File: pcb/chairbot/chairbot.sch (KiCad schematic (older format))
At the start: 18 parts, among them J1 Conn_01x02, J2 Conn_01x05, U1 ESP32mini, U2 74HCT08, U3 74HCT244, U4 buck-converter, U5 nRF24L01+, U8 AMS1117-3.3, U9 PCA9515

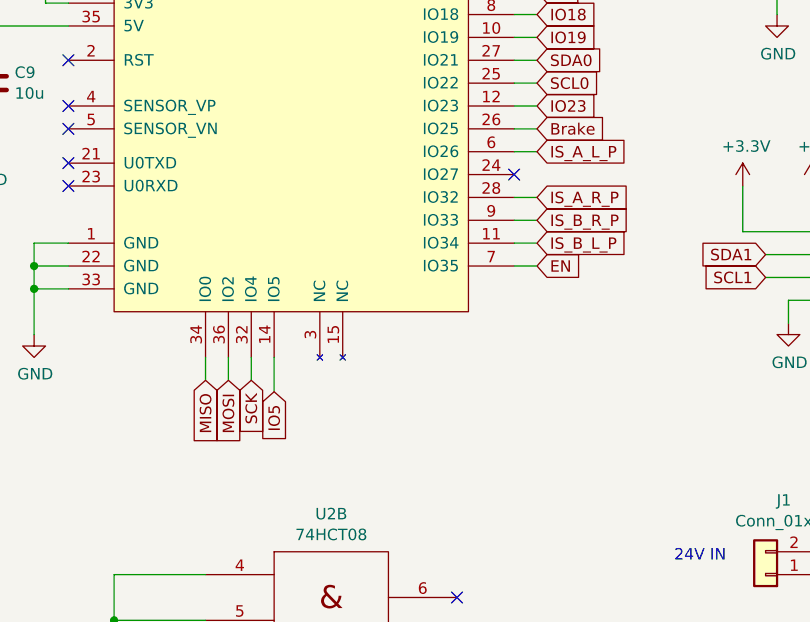
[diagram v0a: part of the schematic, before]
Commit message: Move MISO from IO0 to IO27.
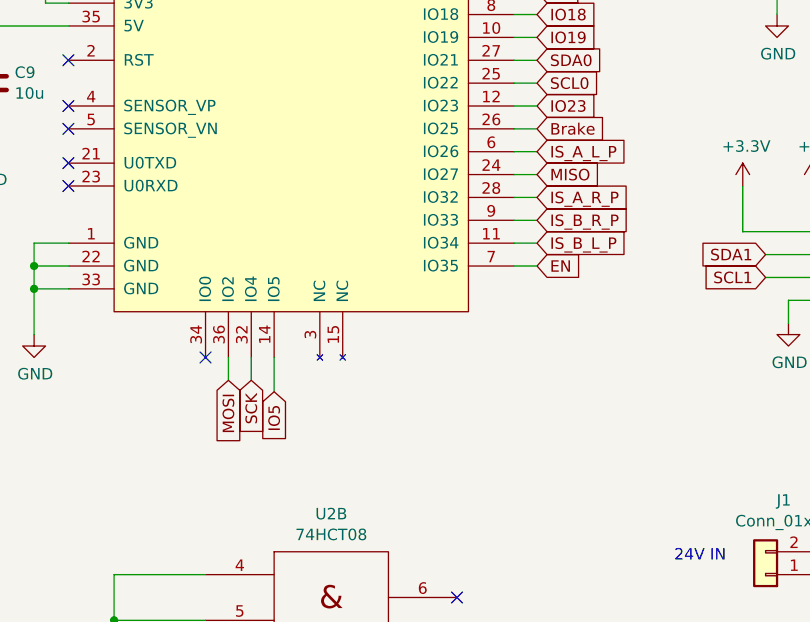
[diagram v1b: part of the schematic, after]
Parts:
- D1: footprint Diode_SMD:D_SMC -> Diode_SMD:D_SMB
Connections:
- net MISO: now also U1.24 (IO27); no longer U1.34 (IO0)
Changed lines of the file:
@@
 F 0 "D1" V 6004 5529 50  0000 L CNN
 F 1 "SS34" V 6095 5529 50  0000 L CNN
-F 2 "Diode_SMD:D_SMC" H 6050 5450 50  0001 C CNN
+F 2 "Diode_SMD:D_SMB" H 6050 5450 50  0001 C CNN
 F 3 "~" H 6050 5450 50  0001 C CNN
 	1    6050 5450
@@
 Text GLabel 2900 4500 3    50   Input ~ 0
 MOSI
-Text GLabel 2800 4500 3    50   Input ~ 0
+Text GLabel 4250 3600 2    50   Input ~ 0
 MISO
 Text GLabel 3000 4500 3    50   Input ~ 0
@@
 	4150 2700 4250 2700
 Wire Wire Line
-	2800 4400 2800 4500
-Wire Wire Line
 	2900 4400 2900 4500
 Wire Wire Line
@@
 NoConn ~ 2200 3550
 NoConn ~ 2200 3650
-NoConn ~ 4150 3600
 $Comp
 L power:+5V #PWR0125
@@
 Wire Wire Line
 	4250 3700 4150 3700
+Wire Wire Line
+	4250 3600 4150 3600
+NoConn ~ 2800 4400
 $EndSCHEMATC

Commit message: Fix various issues.
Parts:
- removed F1: Fuse, Resistor_THT:R_Axial_DIN0309_L9.0mm_D3.2mm_P2.54mm_Vertical, symbol Device:Fuse
- added C11: 100n, Capacitor_SMD:C_0603_1608Metric, symbol Device:C
- added R3: 10K, Resistor_SMD:R_0603_1608Metric, symbol Device:R
- added R4: 1K, Resistor_SMD:R_0603_1608Metric, symbol Device:R
- added R5: 2K2, Resistor_SMD:R_0603_1608Metric, symbol Device:R
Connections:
- net +24V: now also R3.1
- net Brake: now also U1.21 (U0TXD); no longer U1.26 (IO25)
- net EN: now also R5.1
- net GND: now also C11.2, R4.2, R5.2; no longer D1.2 (A)
- net at J1.2 (Pin_2): now also D1.2 (A)
- new net Vbat: C11.1, R3.2, R4.1, U1.26 (IO25)
- no-connect marks 24 -> 23
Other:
- moved on the sheet: C9, D1
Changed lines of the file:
@@
 	5450 5350 5550 5350
 $Comp
-L Device:Fuse F1
-U 1 1 5BD26A01
+L Device:D_Schottky D1
+U 1 1 5BD26B72
 P 5750 5250
-F 0 "F1" V 5553 5250 50  0000 C CNN
-F 1 "Fuse" V 5644 5250 50  0000 C CNN
-F 2 "Resistor_THT:R_Axial_DIN0309_L9.0mm_D3.2mm_P2.54mm_Vertical" V 5680 5250 50  0001 C CNN
+F 0 "D1" V 5704 5329 50  0000 L CNN
+F 1 "SS34" V 5795 5329 50  0000 L CNN
+F 2 "Diode_SMD:D_SMB" H 5750 5250 50  0001 C CNN
 F 3 "~" H 5750 5250 50  0001 C CNN
 	1    5750 5250
-	0    1    1    0
-$EndComp
-$Comp
-L Device:D_Schottky D1
-U 1 1 5BD26B72
-P 6050 5450
-F 0 "D1" V 6004 5529 50  0000 L CNN
-F 1 "SS34" V 6095 5529 50  0000 L CNN
-F 2 "Diode_SMD:D_SMB" H 6050 5450 50  0001 C CNN
-F 3 "~" H 6050 5450 50  0001 C CNN
-	1    6050 5450
-	0    1    1    0
+	-1   0    0    1
 $EndComp
 Wire Wire Line
 	5550 5350 5550 5650
-Wire Wire Line
-	6050 5600 6050 5650
-Wire Wire Line
-	6050 5650 5550 5650
 Connection ~ 5550 5650
 Wire Wire Line
@@
 Wire Wire Line
 	5450 5250 5600 5250
-Wire Wire Line
-	5900 5250 6050 5250
-Wire Wire Line
-	6050 5250 6050 5300
 $Comp
 L power:+24V #PWR03
@@
 	1    0    0    -1
 $EndComp
-Connection ~ 6050 5250
 $Comp
 L buckconverter:buck-converter U4
@@
 	6550 5500 6850 5500
 Wire Wire Line
-	6050 5250 6550 5250
-Wire Wire Line
 	6550 5050 6550 5250
 Connection ~ 6550 5250
-Wire Wire Line
-	6050 5650 6850 5650
-Connection ~ 6050 5650
 $Comp
 L power:+5V #PWR06
@@
 Text GLabel 4250 4000 2    50   Input ~ 0
 EN
-Text GLabel 4250 3400 2    50   Input ~ 0
+Text GLabel 2050 3550 0    50   Input ~ 0
 Brake
 $Comp
@@
 L Device:C C9
 U 1 1 5BD55B4E
-P 1850 3200
-F 0 "C9" H 1965 3246 50  0000 L CNN
-F 1 "10u" H 1965 3155 50  0000 L CNN
-F 2 "Capacitor_SMD:C_0805_2012Metric" H 1888 3050 50  0001 C CNN
-F 3 "~" H 1850 3200 50  0001 C CNN
-	1    1850 3200
+P 1500 3200
+F 0 "C9" H 1615 3246 50  0000 L CNN
+F 1 "10u" H 1615 3155 50  0000 L CNN
+F 2 "Capacitor_SMD:C_0805_2012Metric" H 1538 3050 50  0001 C CNN
+F 3 "~" H 1500 3200 50  0001 C CNN
+	1    1500 3200
 	1    0    0    -1
 $EndComp
@@
 L power:+5V #PWR0122
 U 1 1 5BD55BFD
-P 1850 2850
-F 0 "#PWR0122" H 1850 2700 50  0001 C CNN
-F 1 "+5V" H 1865 3023 50  0000 C CNN
-F 2 "" H 1850 2850 50  0001 C CNN
-F 3 "" H 1850 2850 50  0001 C CNN
-	1    1850 2850
-	1    0    0    -1
-$EndComp
-Wire Wire Line
-	1850 2850 1850 2950
-Wire Wire Line
-	2200 2950 1850 2950
-Connection ~ 1850 2950
-Wire Wire Line
-	1850 2950 1850 3050
+P 1500 2850
+F 0 "#PWR0122" H 1500 2700 50  0001 C CNN
+F 1 "+5V" H 1515 3023 50  0000 C CNN
+F 2 "" H 1500 2850 50  0001 C CNN
+F 3 "" H 1500 2850 50  0001 C CNN
+	1    1500 2850
+	1    0    0    -1
+$EndComp
+Wire Wire Line
+	1500 2850 1500 2950
+Connection ~ 1500 2950
+Wire Wire Line
+	1500 2950 1500 3050
 $Comp
 L power:GND #PWR0123
 U 1 1 5BD59785
-P 1850 3450
-F 0 "#PWR0123" H 1850 3200 50  0001 C CNN
-F 1 "GND" H 1855 3277 50  0000 C CNN
-F 2 "" H 1850 3450 50  0001 C CNN
-F 3 "" H 1850 3450 50  0001 C CNN
-	1    1850 3450
-	1    0    0    -1
-$EndComp
-Wire Wire Line
-	1850 3450 1850 3350
+P 1500 3450
+F 0 "#PWR0123" H 1500 3200 50  0001 C CNN
+F 1 "GND" H 1505 3277 50  0000 C CNN
+F 2 "" H 1500 3450 50  0001 C CNN
+F 3 "" H 1500 3450 50  0001 C CNN
+	1    1500 3450
+	1    0    0    -1
+$EndComp
+Wire Wire Line
+	1500 3450 1500 3350
 $Comp
 L power:+3.3V #PWR0124
@@
 Wire Wire Line
 	4150 3400 4250 3400
-NoConn ~ 2200 3550
 NoConn ~ 2200 3650
 $Comp
@@
 	4250 3600 4150 3600
 NoConn ~ 2800 4400
+Wire Wire Line
+	1500 2950 2200 2950
+Wire Wire Line
+	2050 3550 2200 3550
+Text GLabel 4250 3400 2    50   Input ~ 0
+Vbat
+$Comp
+L Device:R R3
+U 1 1 5CB47065
+P 1250 5900
+F 0 "R3" H 1320 5946 50  0000 L CNN
+F 1 "10K" H 1320 5855 50  0000 L CNN
+F 2 "Resistor_SMD:R_0603_1608Metric" V 1180 5900 50  0001 C CNN
+F 3 "~" H 1250 5900 50  0001 C CNN
+	1    1250 5900
+	1    0    0    -1
+$EndComp
+$Comp
+L Device:R R4
+U 1 1 5CB470D2
+P 1250 6500
+F 0 "R4" H 1320 6546 50  0000 L CNN
+F 1 "1K" H 1320 6455 50  0000 L CNN
+F 2 "Resistor_SMD:R_0603_1608Metric" V 1180 6500 50  0001 C CNN
+F 3 "~" H 1250 6500 50  0001 C CNN
+	1    1250 6500
+	1    0    0    -1
+$EndComp
+$Comp
+L power:+24V #PWR011
+U 1 1 5CB4717B
+P 1250 5550
+F 0 "#PWR011" H 1250 5400 50  0001 C CNN
+F 1 "+24V" H 1265 5723 50  0000 C CNN
+F 2 "" H 1250 5550 50  0001 C CNN
+F 3 "" H 1250 5550 50  0001 C CNN
+	1    1250 5550
+	1    0    0    -1
+$EndComp
+$Comp
+L power:GND #PWR012
+U 1 1 5CB47209
+P 1250 6950
+F 0 "#PWR012" H 1250 6700 50  0001 C CNN
+F 1 "GND" H 1255 6777 50  0000 C CNN
+F 2 "" H 1250 6950 50  0001 C CNN
+F 3 "" H 1250 6950 50  0001 C CNN
+	1    1250 6950
+	1    0    0    -1
+$EndComp
+$Comp
+L Device:C C11
+U 1 1 5CB47282
+P 850 6500
+F 0 "C11" H 965 6546 50  0000 L CNN
+F 1 "100n" H 965 6455 50  0000 L CNN
+F 2 "Capacitor_SMD:C_0603_1608Metric" H 888 6350 50  0001 C CNN
+F 3 "~" H 850 6500 50  0001 C CNN
+	1    850  6500
+	1    0    0    -1
+$EndComp
+Wire Wire Line
+	1250 6050 1250 6200
+Wire Wire Line
+	850  6350 850  6200
+Wire Wire Line
+	850  6200 1250 6200
+Connection ~ 1250 6200
+Wire Wire Line
+	1250 6200 1250 6350
+Wire Wire Line
+	1250 5550 1250 5750
+Wire Wire Line
+	1250 6650 1250 6800
+Wire Wire Line
+	850  6650 850  6800
+Wire Wire Line
+	850  6800 1250 6800
+Connection ~ 1250 6800
+Wire Wire Line
+	1250 6800 1250 6950
+Text GLabel 1500 6200 2    50   Input ~ 0
+Vbat
+Wire Wire Line
+	1500 6200 1250 6200
+$Comp
+L Device:R R5
+U 1 1 5CB60365
+P 4150 4400
+F 0 "R5" H 4220 4446 50  0000 L CNN
+F 1 "2K2" H 4220 4355 50  0000 L CNN
+F 2 "Resistor_SMD:R_0603_1608Metric" V 4080 4400 50  0001 C CNN
+F 3 "~" H 4150 4400 50  0001 C CNN
+	1    4150 4400
+	1    0    0    -1
+$EndComp
+$Comp
+L power:GND #PWR013
+U 1 1 5CB60409
+P 4150 4700
+F 0 "#PWR013" H 4150 4450 50  0001 C CNN
+F 1 "GND" H 4155 4527 50  0000 C CNN
+F 2 "" H 4150 4700 50  0001 C CNN
+F 3 "" H 4150 4700 50  0001 C CNN
+	1    4150 4700
+	1    0    0    -1
+$EndComp
+Wire Wire Line
+	4150 4700 4150 4550
+Wire Wire Line
+	4150 4000 4150 4250
+Connection ~ 4150 4000
+Wire Wire Line
+	5900 5250 6550 5250
+Wire Wire Line
+	5550 5650 6850 5650
 $EndSCHEMATC

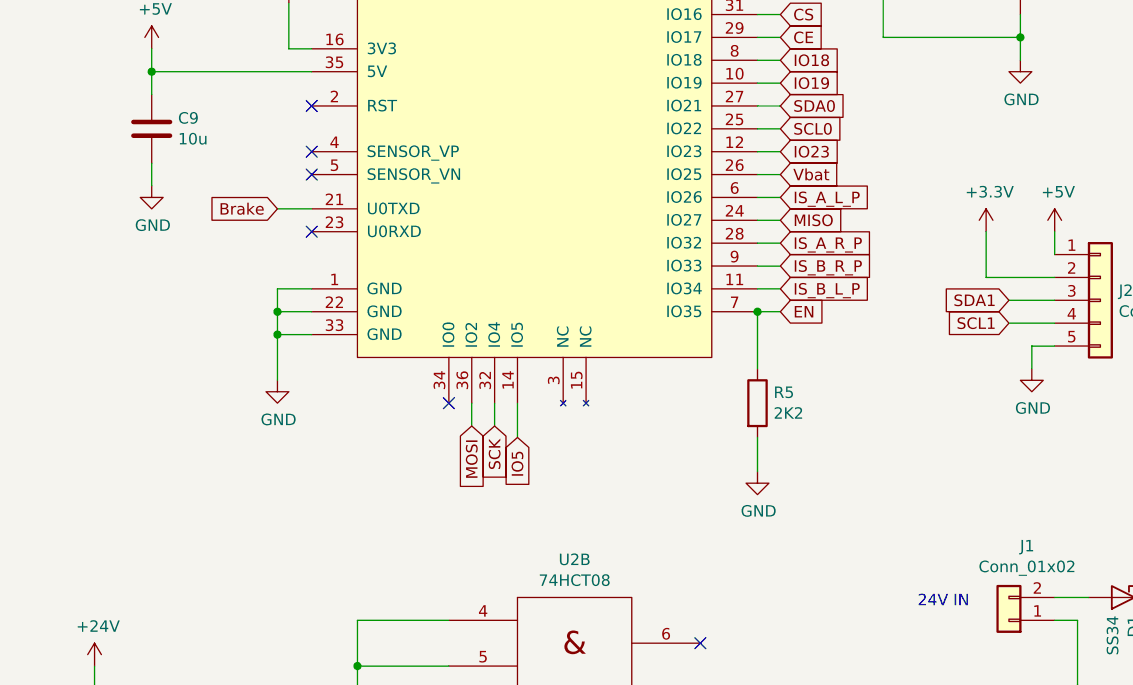
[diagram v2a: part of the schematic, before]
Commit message: Tweak pin numbers.
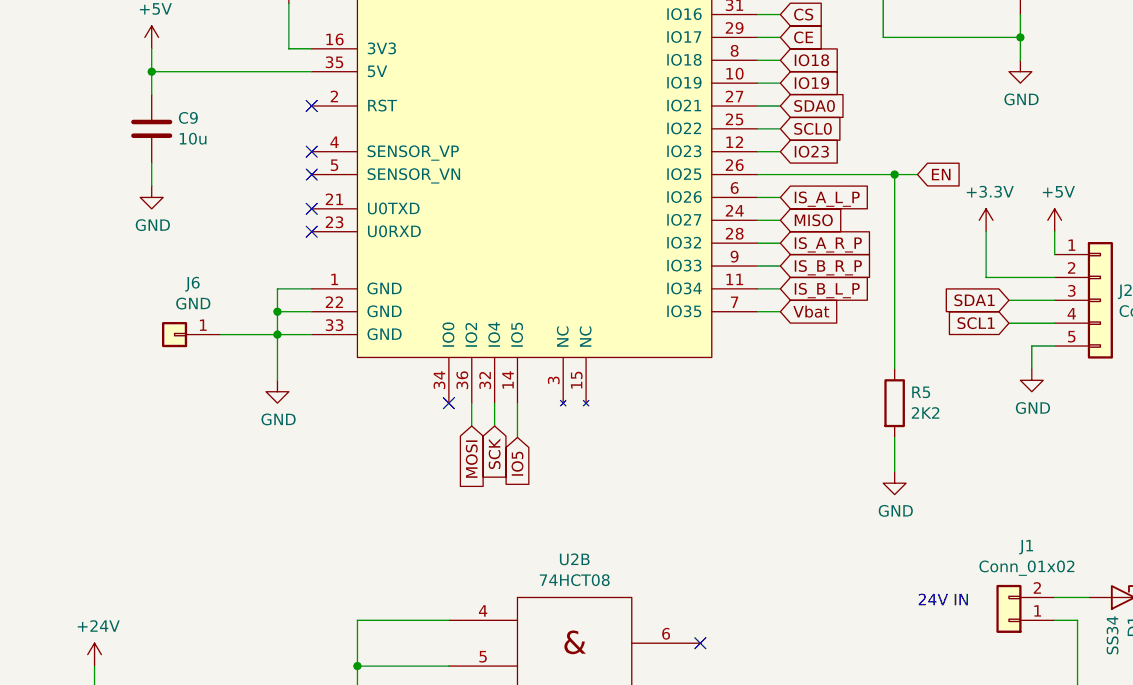
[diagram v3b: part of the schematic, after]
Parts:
- added J6: GND, Connector_Pin:Pin_D1.3mm_L11.0mm, symbol Connector_Generic:Conn_01x01
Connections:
- net EN: now also U1.26 (IO25); no longer U1.7 (IO35)
- net GND: now also J6.1 (Pin_1)
- net Vbat: now also U1.7 (IO35); no longer U1.26 (IO25)
- net Brake: no longer names the net of U1.21 (U0TXD)
- no-connect marks 23 -> 24
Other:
- moved on the sheet: R5
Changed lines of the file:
@@
 EESchema Schematic File Version 4
 LIBS:chairbot-cache
-EELAYER 26 0
+EELAYER 29 0
 EELAYER END
 $Descr A4 11693 8268
@@
 Text GLabel 4250 2800 2    50   Input ~ 0
 CE
-Text GLabel 4250 4000 2    50   Input ~ 0
+Text GLabel 4850 3400 2    50   Input ~ 0
 EN
-Text GLabel 2050 3550 0    50   Input ~ 0
-Brake
 $Comp
 L Regulator_Linear:AMS1117-3.3 U8
@@
 Wire Wire Line
 	4250 4000 4150 4000
-Wire Wire Line
-	4150 3400 4250 3400
 NoConn ~ 2200 3650
 $Comp
@@
 Wire Wire Line
 	1500 2950 2200 2950
-Wire Wire Line
-	2050 3550 2200 3550
-Text GLabel 4250 3400 2    50   Input ~ 0
+Text GLabel 4250 4000 2    50   Input ~ 0
 Vbat
 $Comp
@@
 L Device:R R5
 U 1 1 5CB60365
-P 4150 4400
-F 0 "R5" H 4220 4446 50  0000 L CNN
-F 1 "2K2" H 4220 4355 50  0000 L CNN
-F 2 "Resistor_SMD:R_0603_1608Metric" V 4080 4400 50  0001 C CNN
-F 3 "~" H 4150 4400 50  0001 C CNN
-	1    4150 4400
+P 4750 4400
+F 0 "R5" H 4820 4446 50  0000 L CNN
+F 1 "2K2" H 4820 4355 50  0000 L CNN
+F 2 "Resistor_SMD:R_0603_1608Metric" V 4680 4400 50  0001 C CNN
+F 3 "~" H 4750 4400 50  0001 C CNN
+	1    4750 4400
 	1    0    0    -1
 $EndComp
@@
 L power:GND #PWR013
 U 1 1 5CB60409
-P 4150 4700
-F 0 "#PWR013" H 4150 4450 50  0001 C CNN
-F 1 "GND" H 4155 4527 50  0000 C CNN
-F 2 "" H 4150 4700 50  0001 C CNN
-F 3 "" H 4150 4700 50  0001 C CNN
-	1    4150 4700
-	1    0    0    -1
-$EndComp
-Wire Wire Line
-	4150 4700 4150 4550
-Wire Wire Line
-	4150 4000 4150 4250
-Connection ~ 4150 4000
+P 4750 4700
+F 0 "#PWR013" H 4750 4450 50  0001 C CNN
+F 1 "GND" H 4755 4527 50  0000 C CNN
+F 2 "" H 4750 4700 50  0001 C CNN
+F 3 "" H 4750 4700 50  0001 C CNN
+	1    4750 4700
+	1    0    0    -1
+$EndComp
+Wire Wire Line
+	4750 4700 4750 4550
 Wire Wire Line
 	5900 5250 6550 5250
 Wire Wire Line
 	5550 5650 6850 5650
+Wire Wire Line
+	4150 3400 4750 3400
+Wire Wire Line
+	4750 4250 4750 3400
+Connection ~ 4750 3400
+Wire Wire Line
+	4750 3400 4850 3400
+NoConn ~ 2200 3550
+$Comp
+L Connector_Generic:Conn_01x01 J6
+U 1 1 5CCFD0F5
+P 1600 4100
+F 0 "J6" H 1518 3875 50  0000 C CNN
+F 1 "GND" H 1518 3966 50  0000 C CNN
+F 2 "Connector_Pin:Pin_D1.3mm_L11.0mm" H 1600 4100 50  0001 C CNN
+F 3 "~" H 1600 4100 50  0001 C CNN
+	1    1600 4100
+	-1   0    0    1
+$EndComp
+Wire Wire Line
+	1800 4100 2050 4100
 $EndSCHEMATC

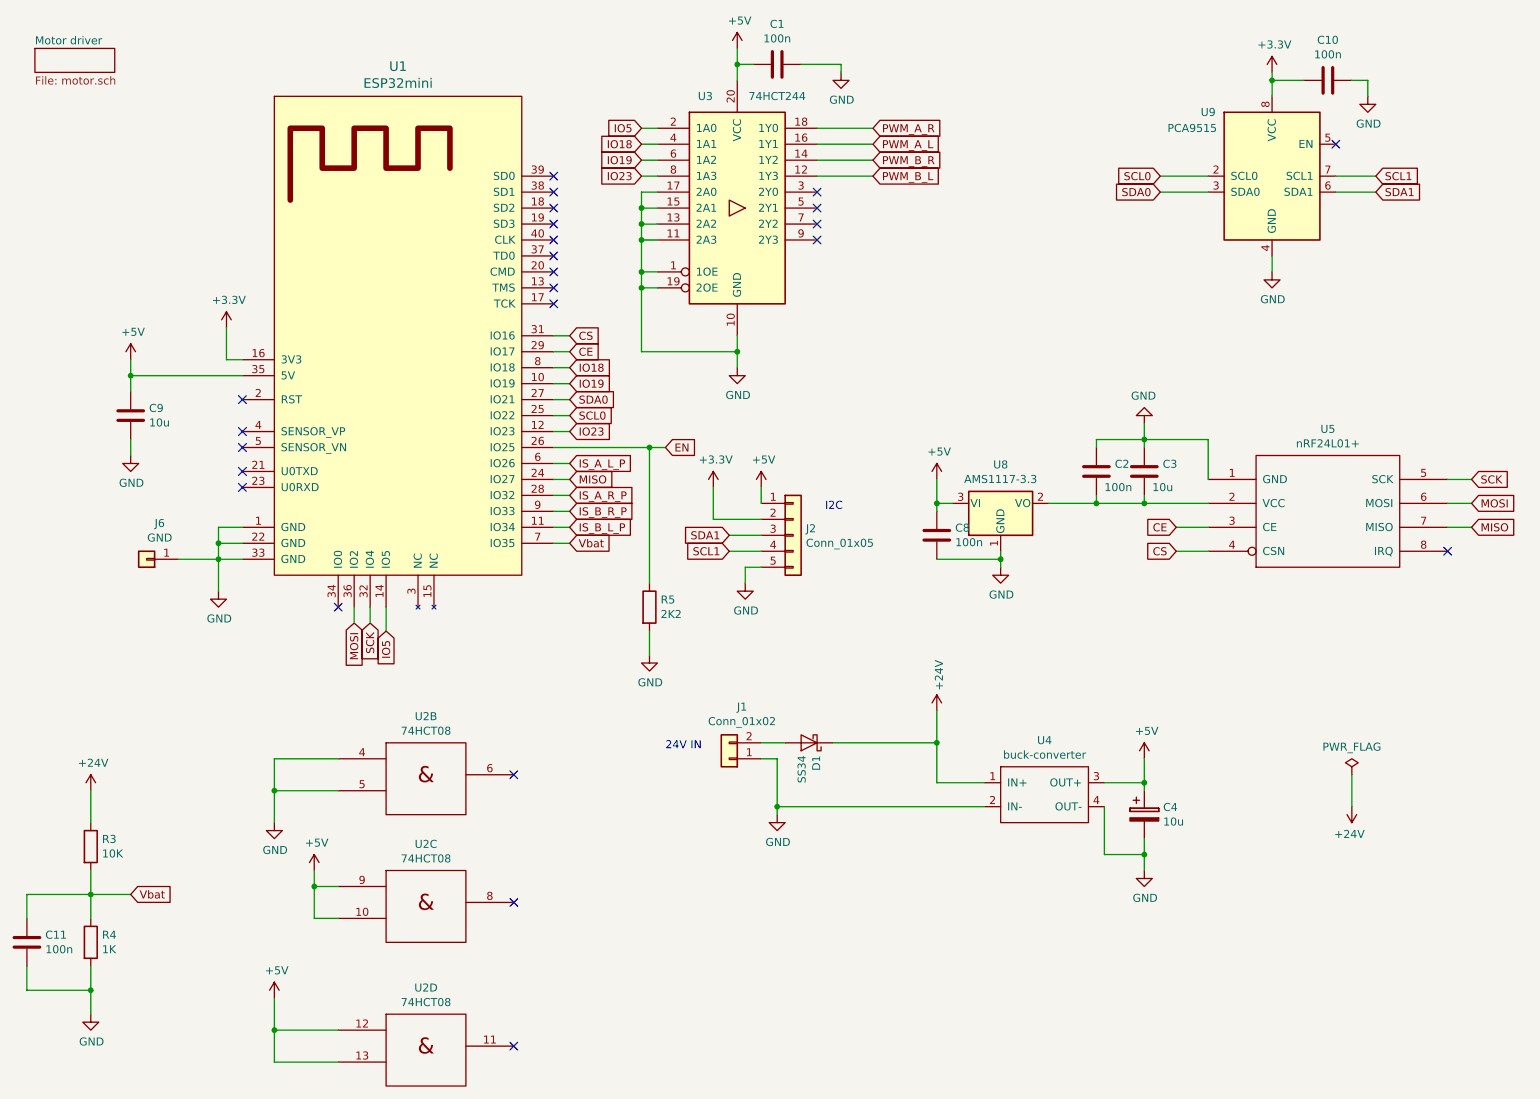
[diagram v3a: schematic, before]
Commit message: Update ADC code for ESP-IDF 5.
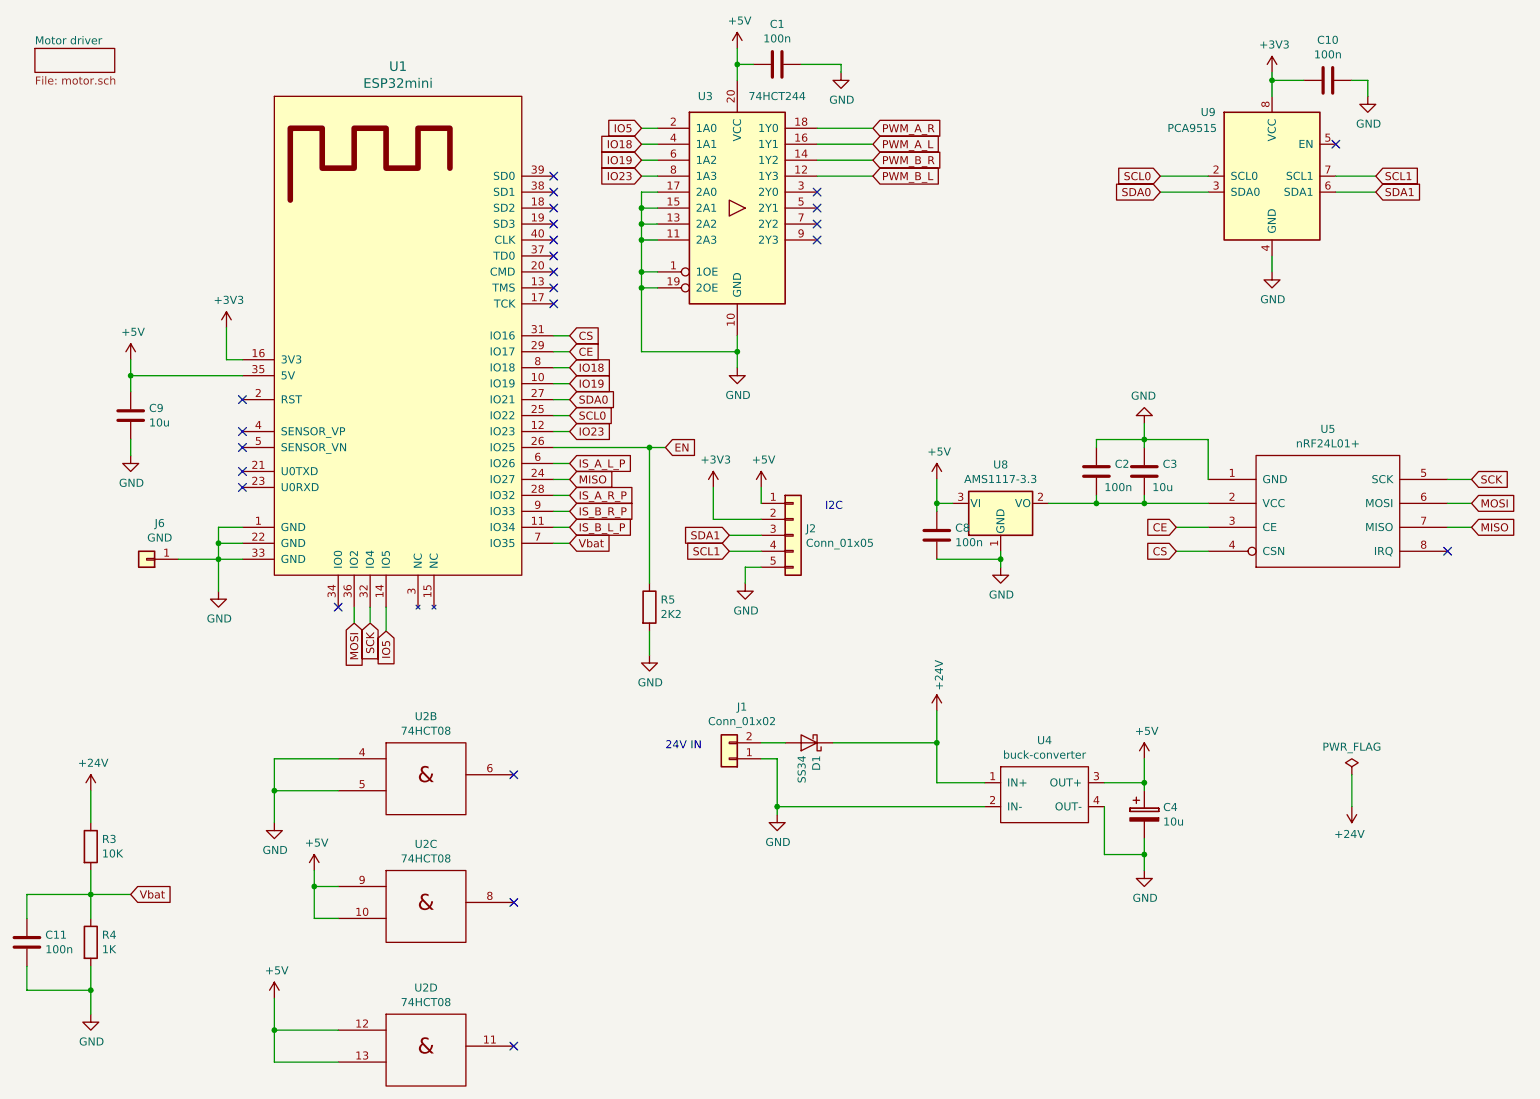
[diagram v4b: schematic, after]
